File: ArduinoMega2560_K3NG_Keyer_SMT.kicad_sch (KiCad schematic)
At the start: 43 parts, among them J10 Conn_01x05_Strip, J11 Conn_01x05_Strip, J12 Conn_01x05_Strip, J13 Conn_01x05_Strip, J2 Conn_01x02, J23 Conn_01x02, J25 Conn_01x05_Strip, J26 Conn_01x05_Strip, J27 Conn_01x05_Strip, J28 Conn_01x05_Strip, J29 Conn_01x05_Strip, J30 Conn_01x05_Strip, J31 Conn_01x05_Strip, J32 Conn_01x05_Strip, J33 Conn_01x05_Strip, J34 Conn_01x05_Strip, J35 Conn_01x05_Strip, J36 Conn_01x05_Strip, J37 Conn_01x05_Strip, J38 Conn_01x05_Strip, J39 Conn_01x05_Strip, J40 Conn_01x05_Strip, J41 Conn_01x05_Strip, J42 Conn_01x05_Strip, J43 Conn_01x05_Strip, J44 Conn_01x05_Strip, J45 Conn_01x05_Strip, J46 Conn_01x05_Strip, J47 Conn_01x05_Strip, J48 Conn_01x05_Strip, J49 Conn_01x05_Strip, J50 Conn_01x05_Strip, J51 Conn_01x05_Strip, J52 Conn_01x05_Strip, J53 Conn_01x05_Strip, J54 Conn_01x05_Strip, J6 Conn_01x05_Strip, J7 Conn_01x05_Strip, J8 Conn_01x05_Strip, J9 Conn_01x05_Strip

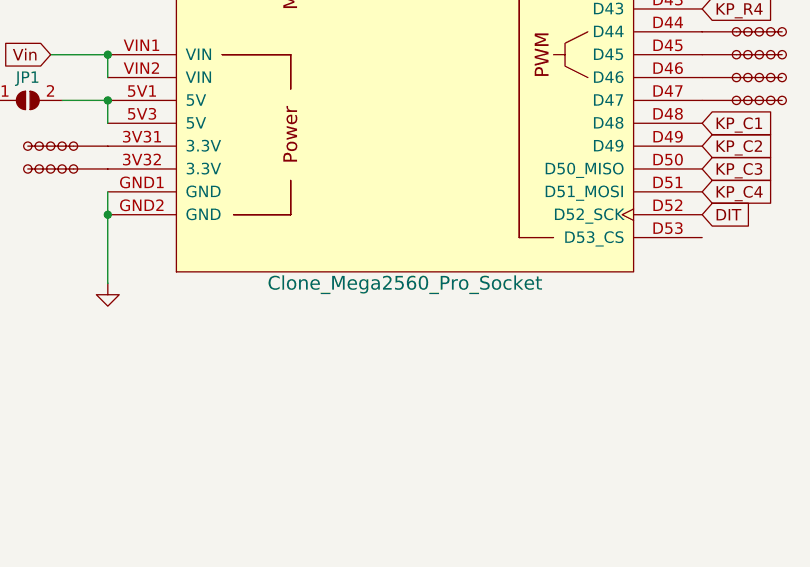
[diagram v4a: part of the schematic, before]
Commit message: First attempt at assigning footprints and JLCPCB part numbers.
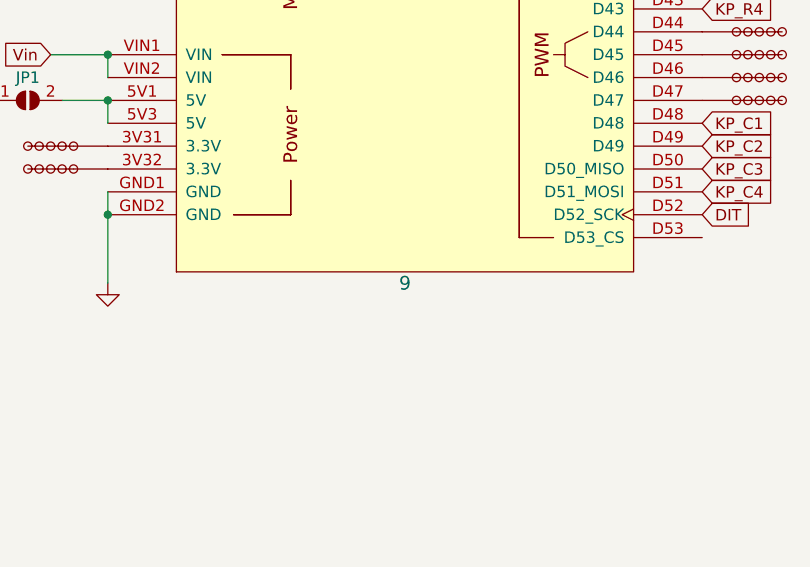
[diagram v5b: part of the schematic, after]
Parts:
- A1: value Clone_Mega2560_Pro_Socket -> 9
- C18: footprint (none) -> Capacitor_SMD:C_Elec_4x5.4; JLCPCB_PN (none) -> C970654
- J10, J11, J12, J13, J25, J26, J27, J28, J29, J30, J31, J32, J33, J34, J35, J36, J37, J38, J39, J40, J41, J42, J43, J44, J45, J46, J47, J48, J49, J50, J51, J52, J53, J54, J6, J7, J8, J9: JLCPCB_PN (none) -> DNP
- J2, J23: footprint (none) -> Connector_PinHeader_2.54mm:PinHeader_1x02_P2.54mm_Vertical; JLCPCB_PN (none) -> DNP
- JP1: footprint (none) -> Jumper:SolderJumper-2_P1.3mm_Open_TrianglePad1.0x1.5mm; JLCPCB_PN (none) -> DNP
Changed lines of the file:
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@@
+      (effects (font (size 1.27 1.27)) hide)
+    )
+    (property "JLCPCB_PN" "DNP" (at 93.98 113.03 0)
       (effects (font (size 1.27 1.27)) hide)
     )
@@
       (effects (font (size 1.27 1.27)))
     )
-    (property "Footprint" "" (at 34.29 60.6552 0)
+    (property "Footprint" "Capacitor_SMD:C_Elec_4x5.4" (at 34.29 60.6552 0)
       (effects (font (size 1.27 1.27)) hide)
     )
@@
       (effects (font (size 1.27 1.27)) hide)
     )
-    (property "JLCPCB_PN" "" (at 38.1 59.69 0)
+    (property "JLCPCB_PN" "C970654" (at 38.1 59.69 0)
       (effects (font (size 1.27 1.27)) hide)
     )
@@
       (effects (font (size 1.27 1.27)) hide)
     )
+    (property "JLCPCB_PN" "DNP" (at 137.16 34.29 0)
+      (effects (font (size 1.27 1.27)) hide)
+    )
     (pin "")
     (instances
@@
       (effects (font (size 1.27 1.27)) hide)
     )
+    (property "JLCPCB_PN" "DNP" (at 167.64 110.49 0)
+      (effects (font (size 1.27 1.27)) hide)
+    )
     (pin "")
     (instances
@@
       (effects (font (size 1.27 1.27)) hide)
     )
+    (property "JLCPCB_PN" "DNP" (at 93.98 102.87 0)
+      (effects (font (size 1.27 1.27)) hide)
+    )
     (pin "")
     (instances
@@
       (effects (font (size 1.27 1.27)) hide)
     )
+    (property "JLCPCB_PN" "DNP" (at 167.64 115.57 0)
+      (effects (font (size 1.27 1.27)) hide)
+    )
     (pin "")
     (instances
@@
       (effects (font (size 1.27 1.27)) hide)
     )
+    (property "JLCPCB_PN" "DNP" (at 93.98 92.71 0)
+      (effects (font (size 1.27 1.27)) hide)
+    )
     (pin "")
     (instances
@@
       (effects (font (size 1.27 1.27)) hide)
     )
+    (property "JLCPCB_PN" "DNP" (at 93.98 110.49 0)
+      (effects (font (size 1.27 1.27)) hide)
+    )
     (pin "")
     (instances
@@
       (effects (font (size 1.27 1.27)) hide)
     )
+    (property "JLCPCB_PN" "DNP" (at 167.64 100.33 0)
+      (effects (font (size 1.27 1.27)) hide)
+    )
     (pin "")
     (instances
@@
       (effects (font (size 1.27 1.27)) hide)
     )
+    (property "JLCPCB_PN" "DNP" (at 93.98 100.33 0)
+      (effects (font (size 1.27 1.27)) hide)
+    )
     (pin "")
     (instances
@@
       (effects (font (size 1.27 1.27)) hide)
     )
+    (property "JLCPCB_PN" "DNP" (at 167.64 143.51 0)
+      (effects (font (size 1.27 1.27)) hide)
+    )
     (pin "")
     (instances
@@
       (effects (font (size 1.27 1.27)) hide)
     )
+    (property "JLCPCB_PN" "DNP" (at 132.08 34.29 0)
+      (effects (font (size 1.27 1.27)) hide)
+    )
     (pin "")
     (instances
@@
       (effects (font (size 1.27 1.27)) hide)
     )
+    (property "JLCPCB_PN" "DNP" (at 93.98 107.95 0)
+      (effects (font (size 1.27 1.27)) hide)
+    )
     (pin "")
     (instances
@@
     )
     (property "Datasheet" "~" (at 127 34.29 0)
+      (effects (font (size 1.27 1.27)) hide)
+    )
+    (property "JLCPCB_PN" "DNP" (at 127 34.29 0)
       (effects (font (size 1.27 1.27)) hide)
     )
@@
       (effects (font (size 1.27 1.27)) hide)
     )
-    (property "Footprint" "" (at 34.29 31.75 0)
+    (property "Footprint" "Connector_PinHeader_2.54mm:PinHeader_1x02_P2.54mm_Vertical" (at 34.29 31.75 0)
       (effects (font (size 1.27 1.27)) hide)
     )
@@
       (effects (font (size 1.27 1.27)) hide)
     )
-    (property "JLCPCB_PN" "" (at 34.29 31.75 0)
+    (property "JLCPCB_PN" "DNP" (at 34.29 31.75 0)
       (effects (font (size 1.27 1.27)) hide)
     )
@@
       (effects (font (size 1.27 1.27)) hide)
     )
+    (property "JLCPCB_PN" "DNP" (at 124.46 34.29 0)
+      (effects (font (size 1.27 1.27)) hide)
+    )
     (pin "")
     (instances
@@
       (effects (font (size 1.27 1.27)) hide)
     )
+    (property "JLCPCB_PN" "DNP" (at 93.98 97.79 0)
+      (effects (font (size 1.27 1.27)) hide)
+    )
     (pin "")
     (instances
@@
     )
     (property "Datasheet" "~" (at 93.98 105.41 0)
+      (effects (font (size 1.27 1.27)) hide)
+    )
+    (property "JLCPCB_PN" "DNP" (at 93.98 105.41 0)
       (effects (font (size 1.27 1.27)) hide)
     )
@@
       (effects (font (size 1.524 1.524)))
     )
-    (property "Value" "Clone_Mega2560_Pro_Socket" (at 130.81 163.83 0)
+    (property "Value" "9" (at 130.81 163.83 0)
       (effects (font (size 1.524 1.524)))
     )
@@
       (effects (font (size 1.27 1.27)) hide)
     )
+    (property "JLCPCB_PN" "DNP" (at 93.98 62.23 0)
+      (effects (font (size 1.27 1.27)) hide)
+    )
     (pin "")
     (instances
@@
       (effects (font (size 1.27 1.27)) hide)
     )
+    (property "JLCPCB_PN" "DNP" (at 93.98 151.13 0)
+      (effects (font (size 1.27 1.27)) hide)
+    )
     (pin "")
     (instances
@@
       (effects (font (size 1.27 1.27)) hide)
     )
+    (property "JLCPCB_PN" "DNP" (at 134.62 34.29 0)
+      (effects (font (size 1.27 1.27)) hide)
+    )
     (pin "")
     (instances
@@
       (effects (font (size 1.27 1.27)) hide)
     )
+    (property "JLCPCB_PN" "DNP" (at 93.98 120.65 0)
+      (effects (font (size 1.27 1.27)) hide)
+    )
     (pin "")
     (instances
@@
       (effects (font (size 1.27 1.27)) hide)
     )
+    (property "JLCPCB_PN" "DNP" (at 167.64 138.43 0)
+      (effects (font (size 1.27 1.27)) hide)
+    )
     (pin "")
     (instances
@@
       (effects (font (size 1.27 1.27)) hide)
     )
+    (property "JLCPCB_PN" "DNP" (at 93.98 95.25 0)
+      (effects (font (size 1.27 1.27)) hide)
+    )
     (pin "")
     (instances
@@
       (effects (font (size 1.27 1.27)) hide)
     )
+    (property "JLCPCB_PN" "DNP" (at 129.54 34.29 0)
+      (effects (font (size 1.27 1.27)) hide)
+    )
     (pin "")
     (instances
@@
       (effects (font (size 1.27 1.27)) hide)
     )
+    (property "JLCPCB_PN" "DNP" (at 93.98 67.31 0)
+      (effects (font (size 1.27 1.27)) hide)
+    )
     (pin "")
     (instances
@@
     )
     (property "Datasheet" "~" (at 167.64 90.17 0)
+      (effects (font (size 1.27 1.27)) hide)
+    )
+    (property "JLCPCB_PN" "DNP" (at 167.64 90.17 0)
       (effects (font (size 1.27 1.27)) hide)
     )
@@
       (effects (font (size 1.27 1.27)) hide)
     )
-    (property "Footprint" "" (at 88.9 143.51 0)
+    (property "Footprint" "Jumper:SolderJumper-2_P1.3mm_Open_TrianglePad1.0x1.5mm" (at 88.9 143.51 0)
       (effects (font (size 1.27 1.27)) hide)
     )
@@
       (effects (font (size 1.27 1.27)) hide)
     )
-    (property "JLCPCB_PN" "" (at 88.9 143.51 0)
+    (property "JLCPCB_PN" "DNP" (at 88.9 143.51 0)
       (effects (font (size 1.27 1.27)) hide)
     )
@@
       (effects (font (size 1.27 1.27)) hide)
     )
+    (property "JLCPCB_PN" "DNP" (at 93.98 87.63 0)
+      (effects (font (size 1.27 1.27)) hide)
+    )
     (pin "")
     (instances
@@
       (effects (font (size 1.27 1.27)) hide)
     )
+    (property "JLCPCB_PN" "DNP" (at 167.64 140.97 0)
+      (effects (font (size 1.27 1.27)) hide)
+    )
     (pin "")
     (instances
@@
     )
     (property "Datasheet" "~" (at 93.98 118.11 0)
+      (effects (font (size 1.27 1.27)) hide)
+    )
+    (property "JLCPCB_PN" "DNP" (at 93.98 118.11 0)
       (effects (font (size 1.27 1.27)) hide)
     )
@@
       (effects (font (size 1.27 1.27)) hide)
     )
-    (property "Footprint" "" (at 26.67 59.69 0)
+    (property "Footprint" "Connector_PinHeader_2.54mm:PinHeader_1x02_P2.54mm_Vertical" (at 26.67 59.69 0)
       (effects (font (size 1.27 1.27)) hide)
     )
@@
       (effects (font (size 1.27 1.27)) hide)
     )
-    (property "JLCPCB_PN" "" (at 26.67 59.69 0)
+    (property "JLCPCB_PN" "DNP" (at 26.67 59.69 0)
       (effects (font (size 1.27 1.27)) hide)
     )
@@
       (effects (font (size 1.27 1.27)) hide)
     )
+    (property "JLCPCB_PN" "DNP" (at 72.39 59.69 0)
+      (effects (font (size 1.27 1.27)) hide)
+    )
     (pin "")
     (instances
@@
       (effects (font (size 1.27 1.27)) hide)
     )
+    (property "JLCPCB_PN" "DNP" (at 93.98 64.77 0)
+      (effects (font (size 1.27 1.27)) hide)
+    )
     (pin "")
     (instances
@@
       (effects (font (size 1.27 1.27)) hide)
     )
+    (property "JLCPCB_PN" "DNP" (at 167.64 135.89 0)
+      (effects (font (size 1.27 1.27)) hide)
+    )
     (pin "")
     (instances
@@
       (effects (font (size 1.27 1.27)) hide)
     )
+    (property "JLCPCB_PN" "DNP" (at 93.98 148.59 0)
+      (effects (font (size 1.27 1.27)) hide)
+    )
     (pin "")
     (instances
@@
       (effects (font (size 1.27 1.27)) hide)
     )
+    (property "JLCPCB_PN" "DNP" (at 93.98 115.57 0)
+      (effects (font (size 1.27 1.27)) hide)
+    )
     (pin "")
     (instances
@@
       (effects (font (size 1.27 1.27)) hide)
     )
+    (property "JLCPCB_PN" "DNP" (at 167.64 49.53 0)
+      (effects (font (size 1.27 1.27)) hide)
+    )
     (pin "")
     (instances
@@
       (effects (font (size 1.27 1.27)) hide)
     )
+    (property "JLCPCB_PN" "DNP" (at 167.64 85.09 0)
+      (effects (font (size 1.27 1.27)) hide)
+    )
     (pin "")
     (instances
@@
       (effects (font (size 1.27 1.27)) hide)
     )
+    (property "JLCPCB_PN" "DNP" (at 93.98 123.19 0)
+      (effects (font (size 1.27 1.27)) hide)
+    )
     (pin "")
     (instances
@@
       (effects (font (size 1.27 1.27)) hide)
     )
+    (property "JLCPCB_PN" "DNP" (at 167.64 80.01 0)
+      (effects (font (size 1.27 1.27)) hide)
+    )
     (pin "")
     (instances
@@
       (effects (font (size 1.27 1.27)) hide)
     )
+    (property "JLCPCB_PN" "DNP" (at 167.64 95.25 0)
+      (effects (font (size 1.27 1.27)) hide)
+    )

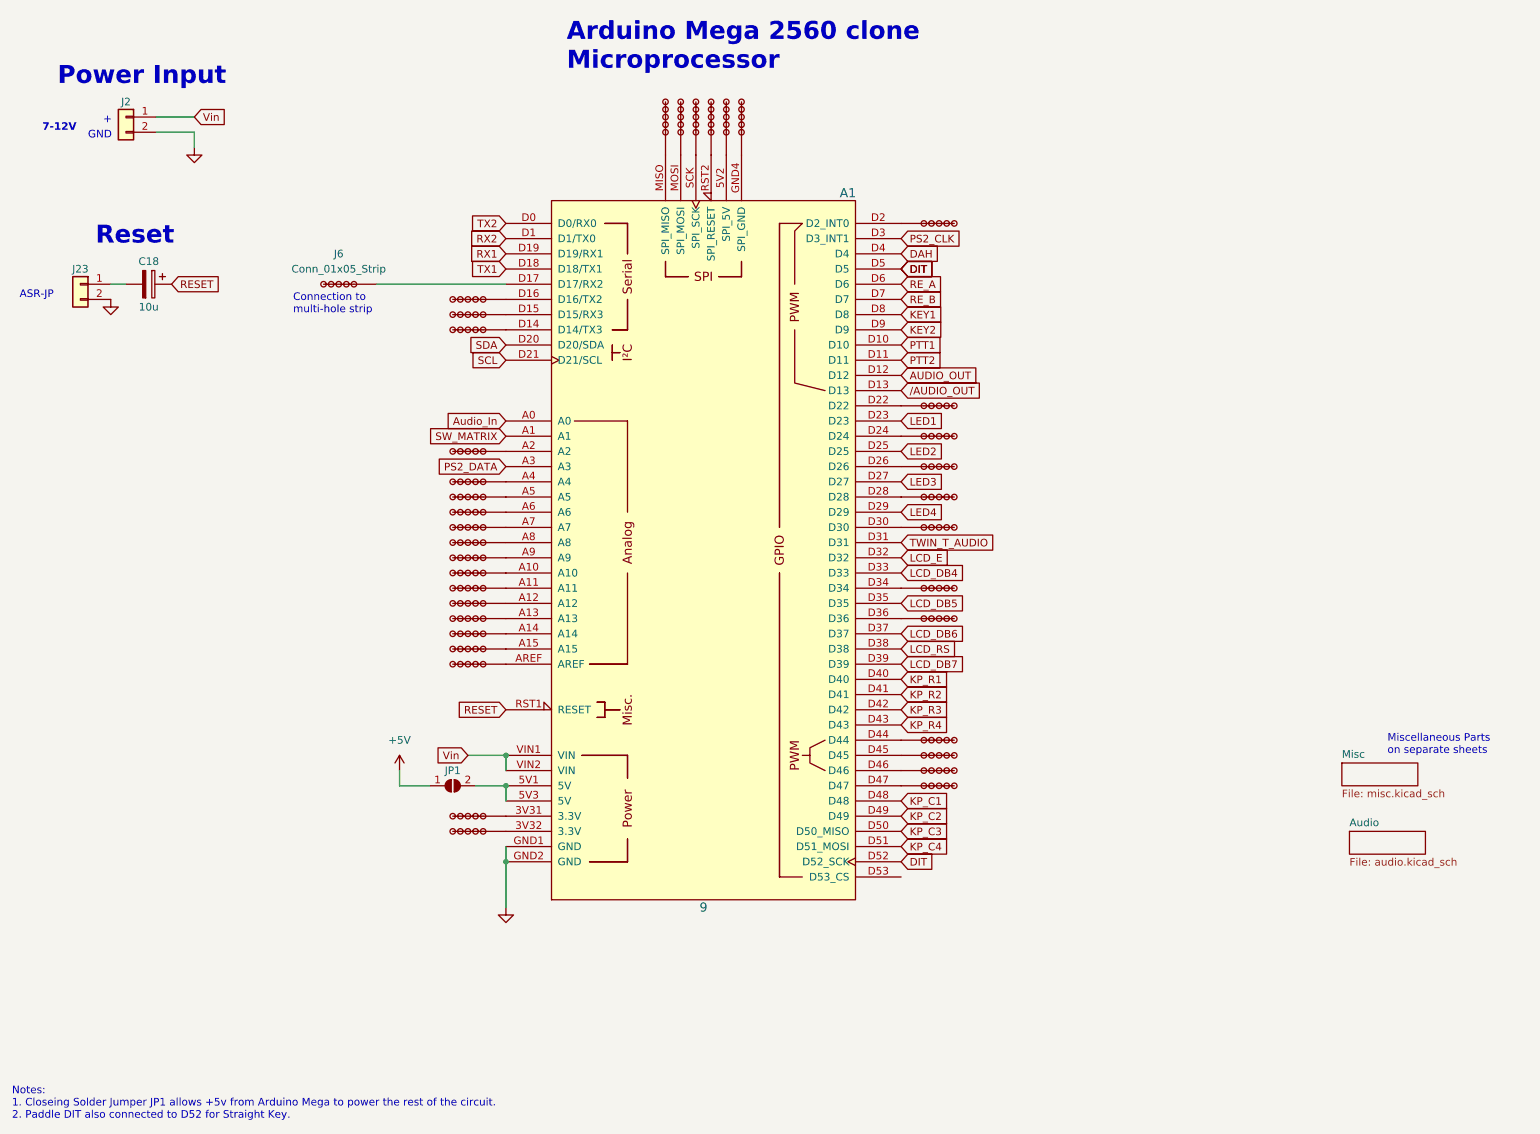
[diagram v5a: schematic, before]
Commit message: Added PWR_FLAG and others to correct ERC errors. All ERC errors corrected; no errors or warnings present.
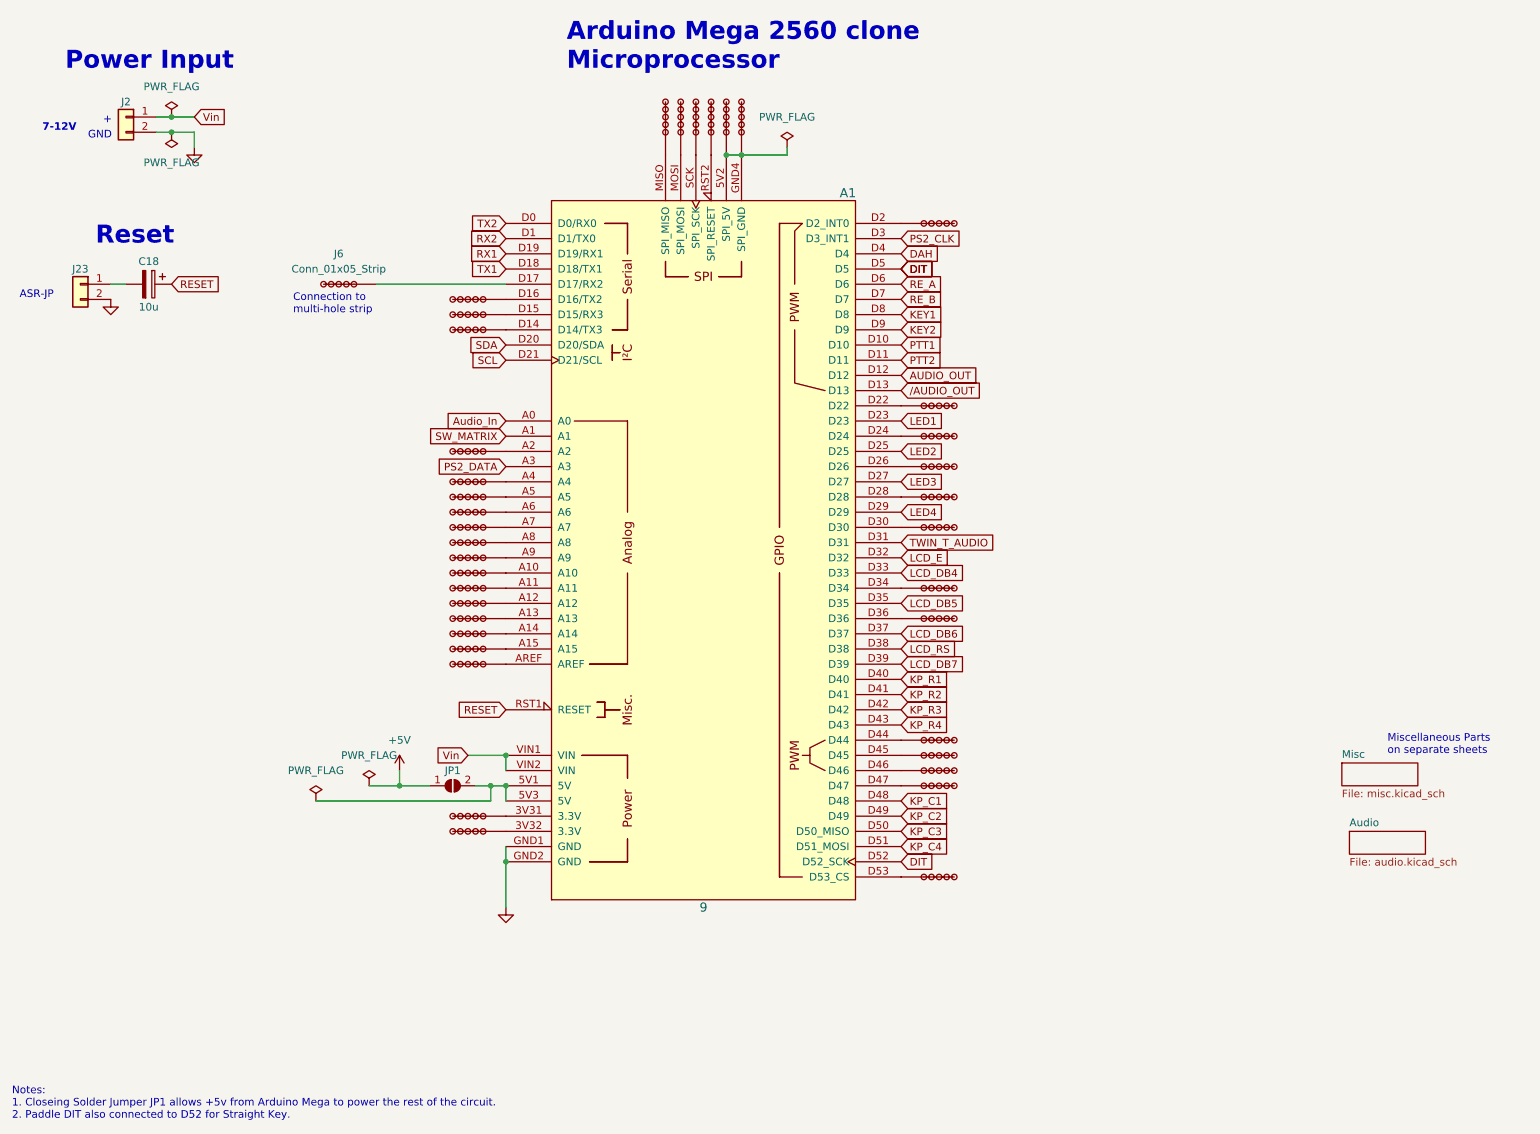
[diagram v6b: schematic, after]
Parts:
- added J56: Conn_01x05_Strip, User:01x05_Strip, symbol User_KICAD6:Conn_01x05_Strip
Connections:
- net at A1.GND4 (SPI_GND), J49. (Pin_1): now also A1.5V2 (SPI_5V), J50. (Pin_1)
- net at A1.D53 (D53_CS): now also J56. (Pin_1)

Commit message: Unknown (minor) changes.
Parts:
- A1: value 9 -> Clone_Mega2560_Pro_Socket; JLCPCB_PN (none) -> DNP
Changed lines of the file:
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@@
       (effects (font (size 1.524 1.524)))
     )
-    (property "Value" "9" (at 130.81 163.83 0)
+    (property "Value" "Clone_Mega2560_Pro_Socket" (at 132.08 163.83 0)
       (effects (font (size 1.524 1.524)))
     )
@@
       (effects (font (size 1.524 1.524)) hide)
     )
-    (property "JLCPCB_PN" "" (at 130.81 104.14 0)
+    (property "JLCPCB_PN" "DNP" (at 130.81 104.14 0)
       (effects (font (size 1.27 1.27)) hide)
     )

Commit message: Changed many capacitor part numbers.
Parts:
- C18: footprint Capacitor_SMD:C_Elec_4x5.4 -> Capacitor_Tantalum_SMD:CP_EIA-1608-08_AVX-J; JLCPCB_PN C970654 -> C1952781
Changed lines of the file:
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@@
       (effects (font (size 1.27 1.27)))
     )
-    (property "Footprint" "Capacitor_SMD:C_Elec_4x5.4" (at 34.29 60.6552 0)
+    (property "Footprint" "Capacitor_Tantalum_SMD:CP_EIA-1608-08_AVX-J" (at 34.29 60.6552 0)
       (effects (font (size 1.27 1.27)) hide)
     )
@@
       (effects (font (size 1.27 1.27)) hide)
     )
-    (property "JLCPCB_PN" "C970654" (at 38.1 59.69 0)
+    (property "JLCPCB_PN" "C1952781" (at 38.1 59.69 0)
       (effects (font (size 1.27 1.27)) hide)
     )
